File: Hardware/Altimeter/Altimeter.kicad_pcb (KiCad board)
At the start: 2 copper layers, 47 x 32 mm, 18 parts, among them J1 Conn_01x06, U1 MS580301BA01-00, U2 MS580301BA01-00, U3 NUP4202

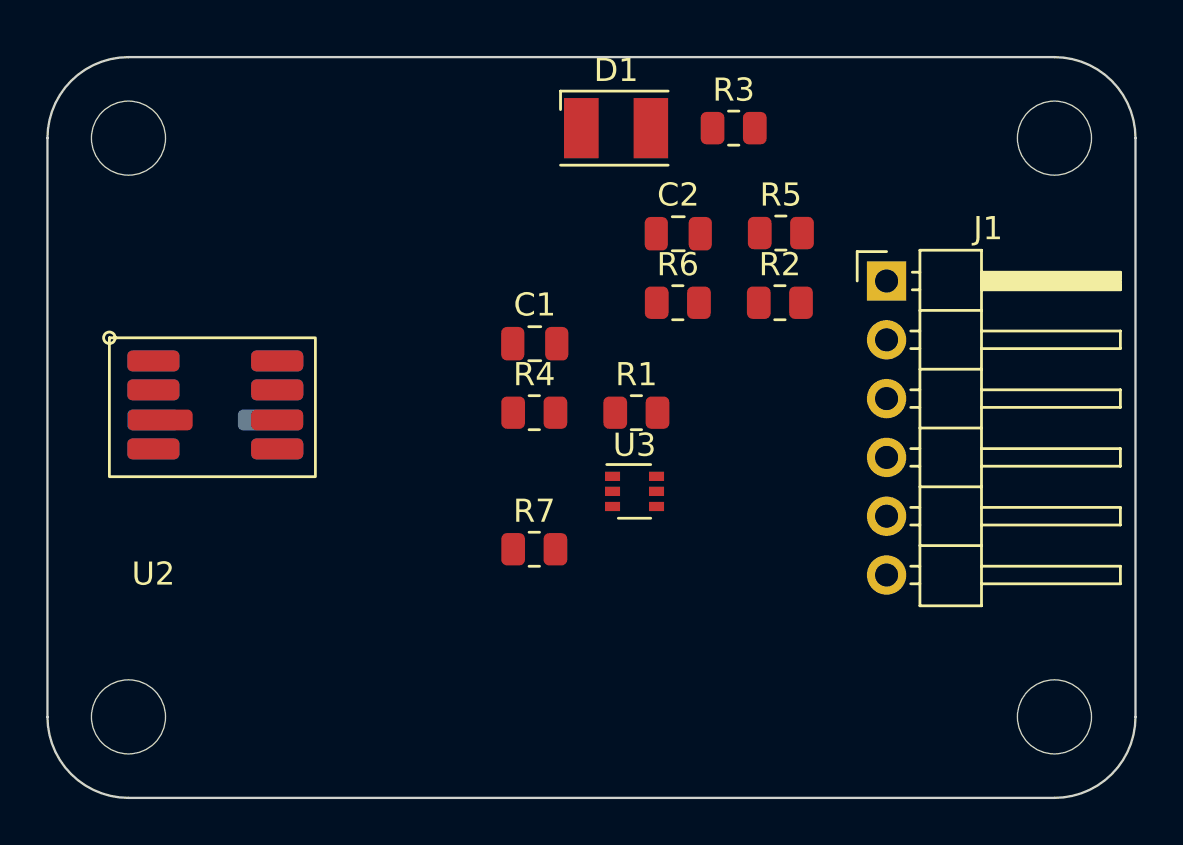
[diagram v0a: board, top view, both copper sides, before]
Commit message: Finished the layout for altimeter
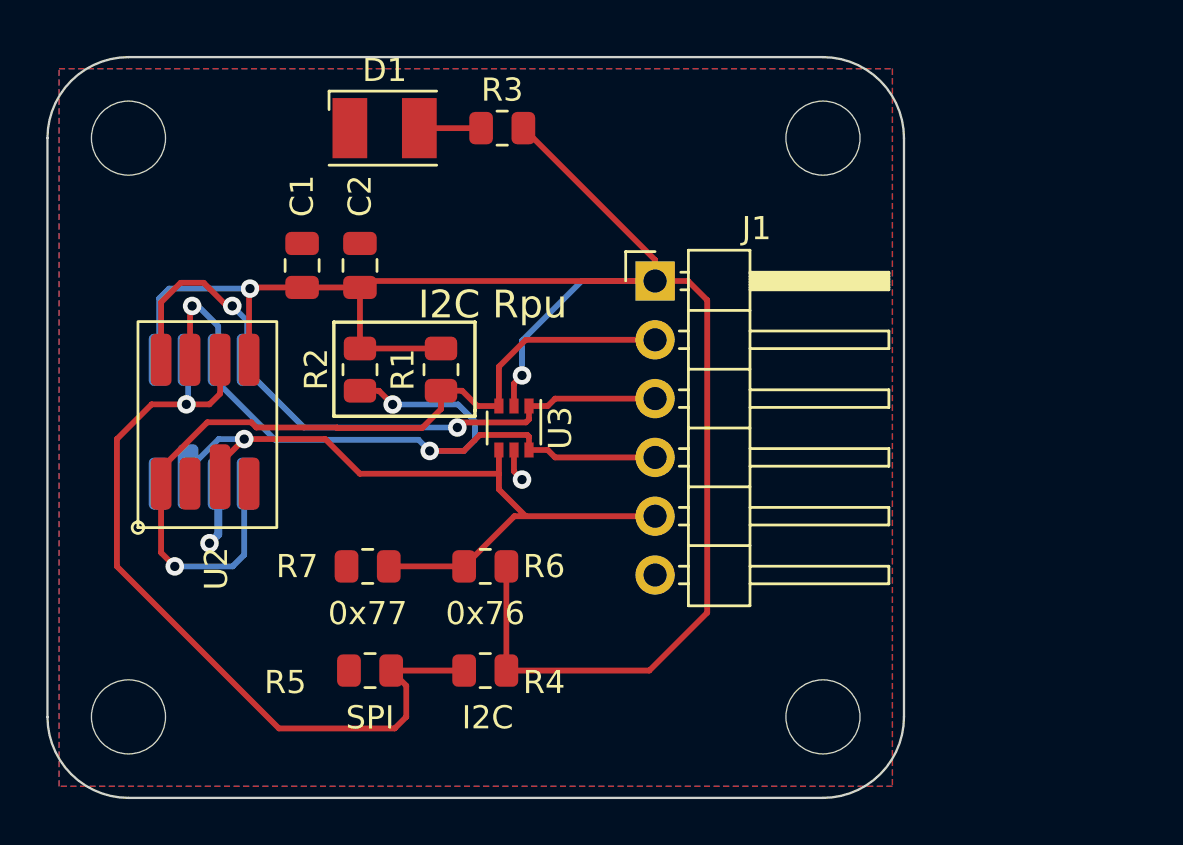
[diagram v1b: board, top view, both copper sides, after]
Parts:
- moved R5 25.9 mm to (120.4, 123.0)
- moved R2 18.4 mm to (120.0, 110.0), turned to 90 degrees
- moved R6 14.1 mm to (125.4, 118.5)
- moved C2 13.8 mm to (120.0, 105.5), turned to 90 degrees
- moved R4 11.3 mm to (125.4, 123.0)
- moved C1 10.6 mm to (117.5, 105.5), turned to 90 degrees
- moved D1 10.0 mm to (121.1, 99.6)
- moved H2 10.0 mm to (140.0, 100.0)
- moved H3 10.0 mm to (140.0, 125.0)
- moved J1 10.0 mm to (132.7, 106.2)
- moved R3 10.0 mm to (126.1, 99.6)
- moved R1 8.64 mm to (123.5, 110.0), turned to 90 degrees
- moved R7 7.24 mm to (120.3, 118.5)
- moved U3 5.88 mm to (126.7, 112.5), turned to -90 degrees
- moved U1 5.46 mm to (115.1, 114.9), turned to 90 degrees
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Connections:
- U3 pad 1: /SCLK -> /SDO
- U3 pad 3: /CSB -> /SCLK
- U3 pad 4: /SDO -> /CSB
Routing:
- net VDD: track 0.00 -> 82.7 mm, vias 0 -> 2
- net /SCLK: track 0.00 -> 36.7 mm, vias 0 -> 1
- net /SDI: track 0.00 -> 36.5 mm, vias 0 -> 3
- net /PS: track 0.00 -> 35.2 mm, vias 0 -> 1
- net /CSB: track 0.00 -> 32.7 mm, vias 0 -> 1
- net /SDO: track 0.00 -> 28.9 mm, vias 0 -> 2
- net GND: track 0.00 -> 4.15 mm, vias 0 -> 2
- net Net-(D1-Pad2): track 0.00 -> 2.67 mm
- added copper zone on B.Cu, net GND
- added copper zone on F.Cu, net GND
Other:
- board size 47 x 32 mm -> 37 x 32 mm
- board text added: "0x76"
- board text added: "0x77"
- board text added: "I2C"
- board text added: "I2C Rpu"
- board text added: "SPI"

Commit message: Last version of altimeter and ACS7111 pcbs
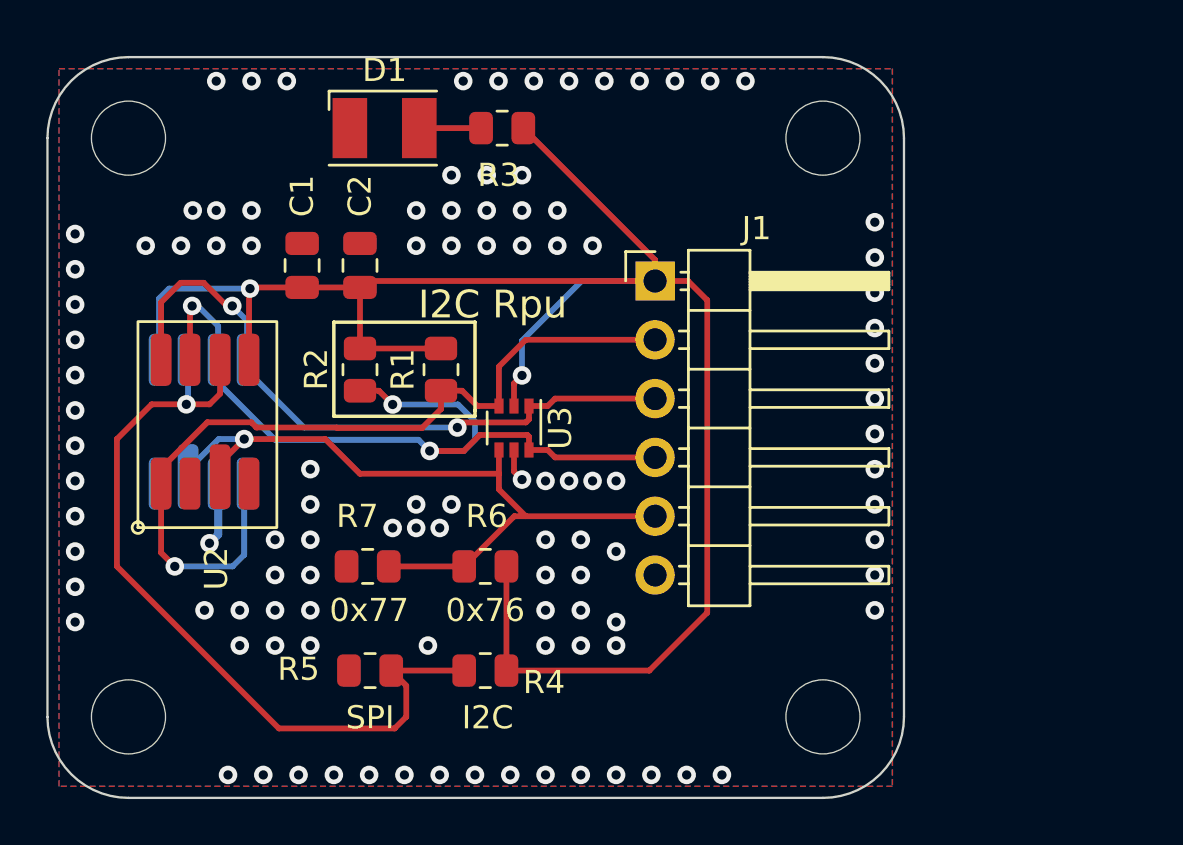
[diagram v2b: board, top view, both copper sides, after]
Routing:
- net GND: vias 2 -> 108

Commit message: update to altimeter pcb
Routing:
- net /PS: track 35.2 -> 34.3 mm
- net VDD: track 82.7 -> 83.5 mm
- net /CSB: track 32.7 -> 33.4 mm
- net GND: vias 108 -> 106
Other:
- board text added: "3v3"
- board text added: "CSB"
- board text added: "GND"
- board text added: "MS5803-xx Altimeter"
- board text added: "SCL"
- board text added: "SDA/SDI"
- board text added: "SDO"
- board text added: "SomethingAboutElectronics 2023 LV/SE"
